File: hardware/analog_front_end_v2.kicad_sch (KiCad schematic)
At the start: 154 parts, among them J1 Conn_Coaxial, J3 Conn_01x01_Socket, J4 Conn_01x01_Socket, T1 WBC1-1TL 1:1, U1 ADL5531, U10 MAX6002, U11 LP2985-5.0, U12 ADF4531, U14 LP2985-5.0, U15 LP2985-5.0, U17 LP2985-3.3, U18 PAT1220-C-0DB, U19 PAT1220-C-0DB, U2 ADL5531, U20 PAT1220-C-0DB, U21 PAT1220-C-0DB, U22 MCP6286, U23 PMOD 2x6 2.54mm pitch, U24 LT5560, U25 LTC6362, U26 LTC6362, U3 ADL5531, U4 ADL5531, U5 LP2985-1.8, U6 MCP33131, U7 PAT1220-C-0DB, U9 PMOD 2x6 2.54mm pitch, Y1 12.8MHz TCXO

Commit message: Further schematic cleanups
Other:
- note removed: "TODO: Recheck if this gain amount is correct for the new downmixer and ADC"
- moved on the sheet: C10, C11, C12, C13, C14, C15, C16, C17, C18, C19, C2, C20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

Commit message: Further refinements/cleanup to Downmixer schematic section
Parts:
- removed C84: 10n, Capacitor_SMD:C_0402_1005Metric, symbol Device:C
- removed C85: 10u, Capacitor_SMD:C_0402_1005Metric, symbol Device:C
- removed C86: 100n, Capacitor_SMD:C_0402_1005Metric, symbol Device:C
- removed TP23: LOCK_DET, TestPoint:TestPoint_Pad_D1.0mm, symbol Connector:TestPoint
- added C22: 1u_16V, Capacitor_SMD:C_0603_1608Metric, symbol Device:C
- added C50: 10u_16V, Capacitor_SMD:C_0805_2012Metric, symbol Device:C
- added C51: 10n_25V, Capacitor_SMD:C_0402_1005Metric, symbol Device:C
- C87, C92, C93, C94: value 100n -> 100n_25V; MOC (none) -> GCM155R71E104KE02D; Size (none) -> 0402; Tolerance (none) -> 5%
- C88: value 1u -> 100n_25V; MOC (none) -> GCM155R71E104KE02D; Size (none) -> 0402; Tolerance (none) -> 5%
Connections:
- net 3V3: now also C22.1; no longer C88.1
- net ADC_SDO: no longer U23.7
- net GND: now also C22.2, C50.1, C51.1
- net PLL_TEMP: now also C93.1; no longer C94.1
- net PLL_VCOM: now also C92.1; no longer C93.1
- net PLL_VREF: now also C88.1; no longer C92.1
- net at FB1.1, U15.5 (VOUT): now also C94.1, C50.2
- net VCO_LD: now reaches U12.25 (LD)
- net VCO_LD: now also U23.7
- net at U15.4 (BP): now also C51.2
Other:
- note added: "Always on, don't care about power drain..."
- note added: "Goals: 1. Cover typical FM range 88 to 108MHz with 95 to 105 best covered 2. Support from -100dBm received signal 3. 50 ohm impedance 4. Minimize parasitics (inc trace resistance) as much as possible in layout 5. Short traces with minimal direction changes"
- note added: "TODO: Assign parts and tolerances!"
- note removed: "EN > 2V for ON"
- note removed: "Goals: 1. Support from -95dBm received signal 2. 50 ohm impedance 3. Minimize parasitics (inc trace resistance) as much as possible in layout 4. Short traces with minimal direction changes"
- note removed: "V_CM buffered by U22 (MCP6286)"
- moved on the sheet: C1, C10, C11, C12, C13, C14, C15, C16, C17, C18, C19, C2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

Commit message: Assign more values to downmixer and butterworth filters
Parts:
- removed C61, C62: 10n, Capacitor_SMD:C_0402_1005Metric, symbol Device:C
- removed C64, C67: 1n, Capacitor_SMD:C_0402_1005Metric, symbol Device:C
- removed C65, C66, C68, C80, C82: 100n, Capacitor_SMD:C_0402_1005Metric, symbol Device:C
- removed C69, C78, C79, C81, C83: 1u, Capacitor_SMD:C_0402_1005Metric, symbol Device:C
- added C23, C26, C29, C37, C39: 1u_16V, Capacitor_SMD:C_0603_1608Metric, symbol Device:C
- added C24, C25: 1n_50V, Capacitor_SMD:C_0402_1005Metric, symbol Device:C
- added C34, C35: 10n_25V, Capacitor_SMD:C_0402_1005Metric, symbol Device:C
- added C95, C96, C97, C98, C99: 100n_25V, Capacitor_SMD:C_0402_1005Metric, symbol Device:C
- C59: MOC (none) -> 0402N270FW201-T500; Size (none) -> 0402; Tolerance (none) -> 1%
- L13, L14: MOC (none) -> LQW15AN18NG8ZD; Tolerance (none) -> 2%
- R32: MOC (none) -> RC0402FR-13162RL; Size (none) -> 0402; Tolerance (none) -> 1%
- R33, R34: MOC (none) -> RC0402FR-07330RL; Size (none) -> 0402; Tolerance (none) -> 1%
- R35, R36, R37, R38, R41, R42, R43, R44: MOC (none) -> RT0402BRD071KL; Size (none) -> 0402; Tolerance (none) -> 1%
- T1: MOC (none) -> ADT1-1+
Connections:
- net 5V_MIX: now also C23.1, C24.1, C37.1, C39.1, C97.1, C98.1, C99.1
- net ADC_VCM: now also C29.1
- net GND: now also C23.2, C24.2, C26.2, C29.2, C35.1, C37.2, C39.2, C97.2, C98.2, C99.2
- net IF_N: now also C95.2
- net IF_P: now also C96.2
- net VCM_DIV: now also C26.1
- net at C63.2, R32.1: now also C34.2
- net at U24.1 (LO-): now also C34.1
- net at R33.2, U24.6 (OUT+): now also C25.1, C96.1
- net at R34.1, U24.5 (OUT-): now also C25.2, C95.1
- net at U24.8 (LO+): now also C35.2
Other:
- note added: "TODO: Assign Ferrite part!"
- note added: "TODO: Create footprint!"
- moved on the sheet: C1, C10, C11, C12, C13, C14, C15, C16, C17, C18, C19, C2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

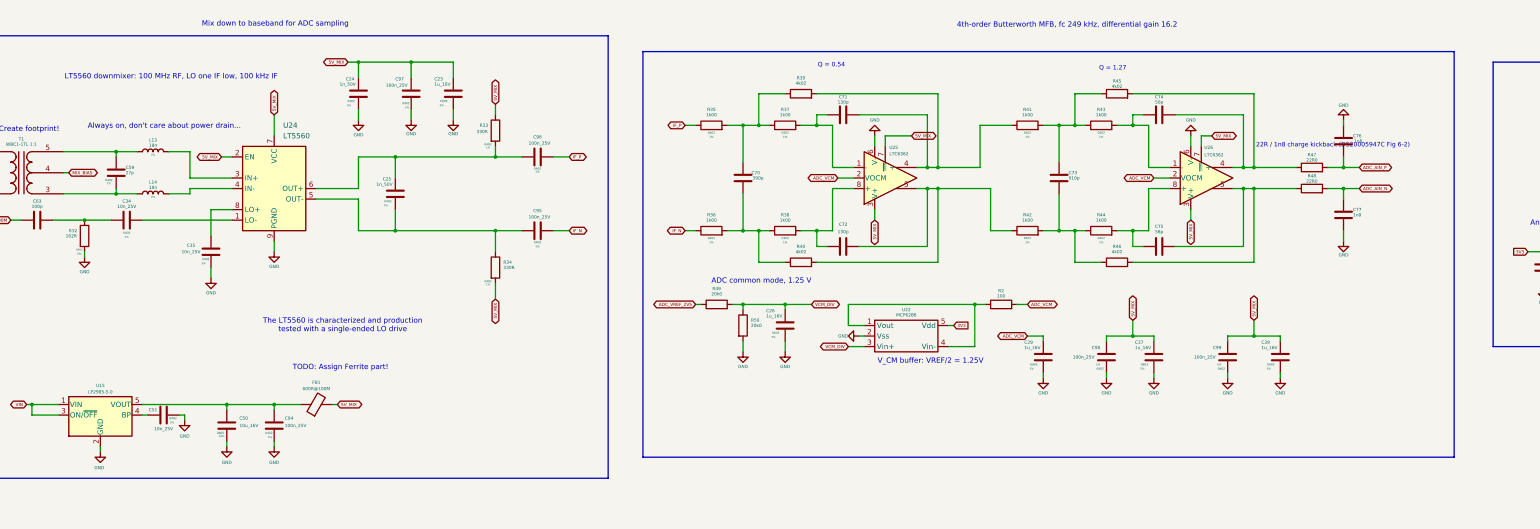
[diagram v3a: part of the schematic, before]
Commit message: Populate more components
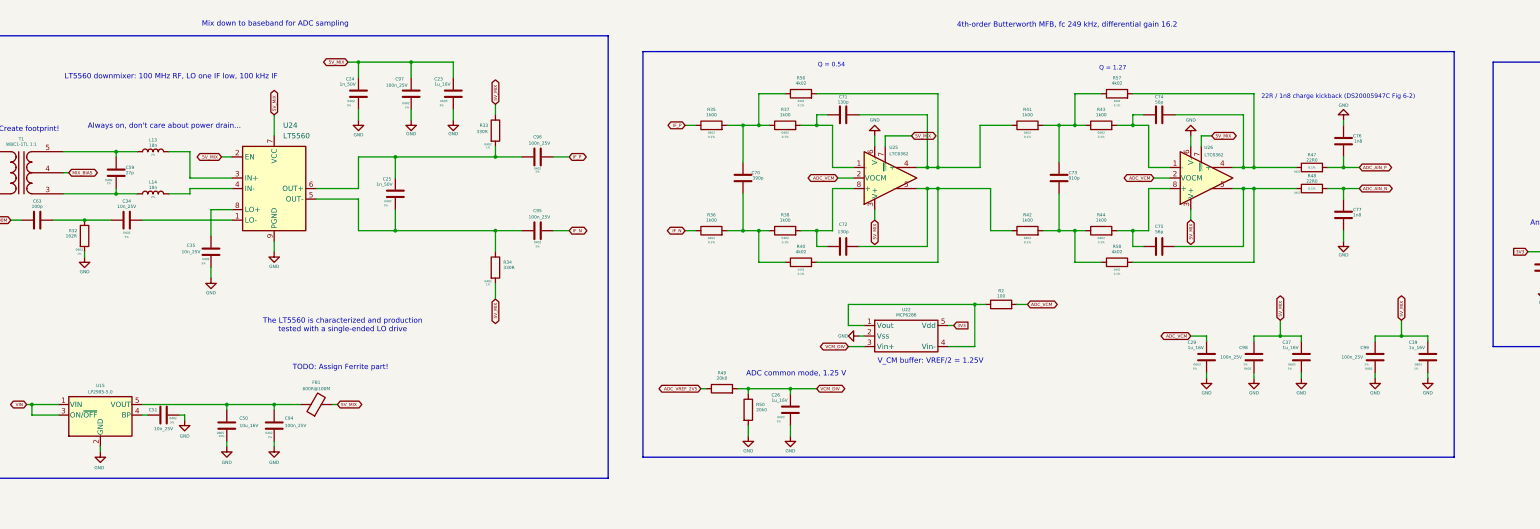
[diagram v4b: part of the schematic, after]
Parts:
- removed R39, R45, R46: 4k02, Resistor_SMD:R_0402_1005Metric, symbol Device:R
- added R56, R57, R58: 4k02, Resistor_SMD:R_0402_1005Metric, symbol Device:R
- R35, R36, R37, R38, R41, R42, R43, R44: Tolerance 1% -> 0.1%
- R40: MOC (none) -> RT0402BRD074K02L; Size (none) -> 0402; Tolerance (none) -> 0.1%
- R47, R48: MOC (none) -> RT0402BRD0722RL; Size (none) -> 0402; Tolerance (none) -> 0.1%
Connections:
- net at C73.2, R42.2, R44.1: now also R58.1
- net at C70.1, R35.2, R37.1: now also R56.1
- net at C71.2, R41.1, U25.4 (+): now also R56.2
- net at C73.1, R41.2, R43.1: now also R57.1
- net at C75.2, R48.1, U26.5 (-): now also R58.2
- net at C74.2, R47.1, U26.4 (+): now also R57.2
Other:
- moved on the sheet: C26, C29, C37, C39, C98, C99, R49, R50

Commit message: Populate more components
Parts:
- removed FB1: 600R@100M, Inductor_SMD:L_0402_1005Metric, symbol Device:FerriteBead
- removed R51: 50R, Resistor_SMD:R_0402_1005Metric, symbol Device:R
- added R59: 50R, Resistor_SMD:R_0402_1005Metric, symbol Device:R
- C70: MOC (none) -> GCM1555C1H391FA16D; Size (none) -> 0402; Tolerance (none) -> 1%
- C71, C72: MOC (none) -> GRT1555C1H131FA02D; Size (none) -> 0402; Tolerance (none) -> 1%
- C73: MOC (none) -> GCM1555C1H911FA16J; Size (none) -> 0402; Tolerance (none) -> 1%
- C74, C75: MOC (none) -> GCM1555C1H560FA16D; Size (none) -> 0402; Tolerance (none) -> 0.1%
- L13, L14: Size (none) -> 0402
- R52: MOC (none) -> RN73R1ETTP50R0F50; Size (none) -> 0402; Tolerance (none) -> 1%
- R53: MOC (none) -> RT0402BRD0733RL; Size (none) -> 0402; Tolerance (none) -> 0.1%
- R54: MOC (none) -> ERA-2AEB1371X; Size (none) -> 0402; Tolerance (none) -> 0.1%
- R55: MOC (none) -> RT0402BRD076K19L; Size (none) -> 0402; Tolerance (none) -> 0.1%
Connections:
- net 3V3: now also R59.1
- net 5V_MIX: now also C50.2, C94.1, U15.5 (VOUT)
- net LO_100M: now also R59.2
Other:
- note removed: "TODO: Assign Ferrite part!"
- moved on the sheet: C23, C24, C35, C95, C96, C97, R34

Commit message: Update more passive MOC/Size/tolerances across the schematic
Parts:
- C76, C77: MOC (none) -> GRM1885C1H182JA01D; Size (none) -> 0603; Tolerance (none) -> 5%
- R2: Size (none) -> 0402; Tolerance (none) -> 0.1%
- R49, R50: MOC (none) -> RC0402FR-0720KL; Size (none) -> 0402; Tolerance (none) -> 1%
- T1: footprint (none) -> fm-radio-footprint-lib:WBC1-1TLC; MOC ADT1-1+ -> WBC1-1TLC
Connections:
- net GND: now also R50.1; no longer R50.2
- net VCM_DIV: now also R50.2; no longer R50.1
- no-connect marks 29 -> 30
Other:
- moved on the sheet: C1, C2, C3, C4, C5, J1, L1, L2, L3, L4, L5, R32

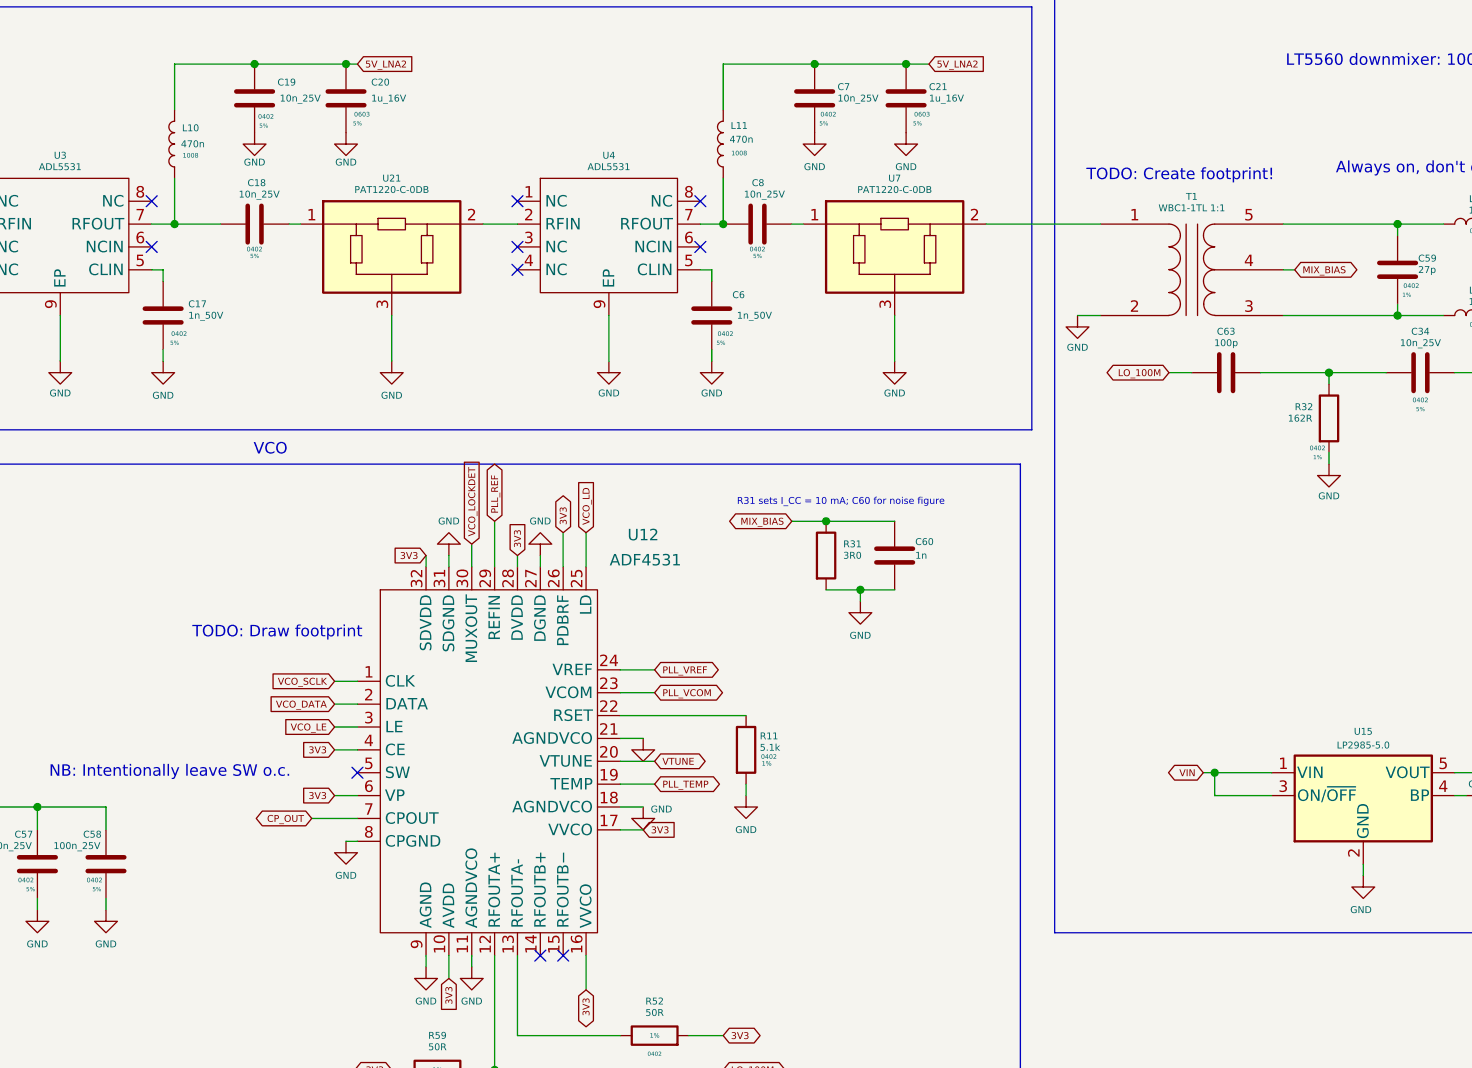
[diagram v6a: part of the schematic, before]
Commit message: More routing and move frontend inductor to be perpendicular
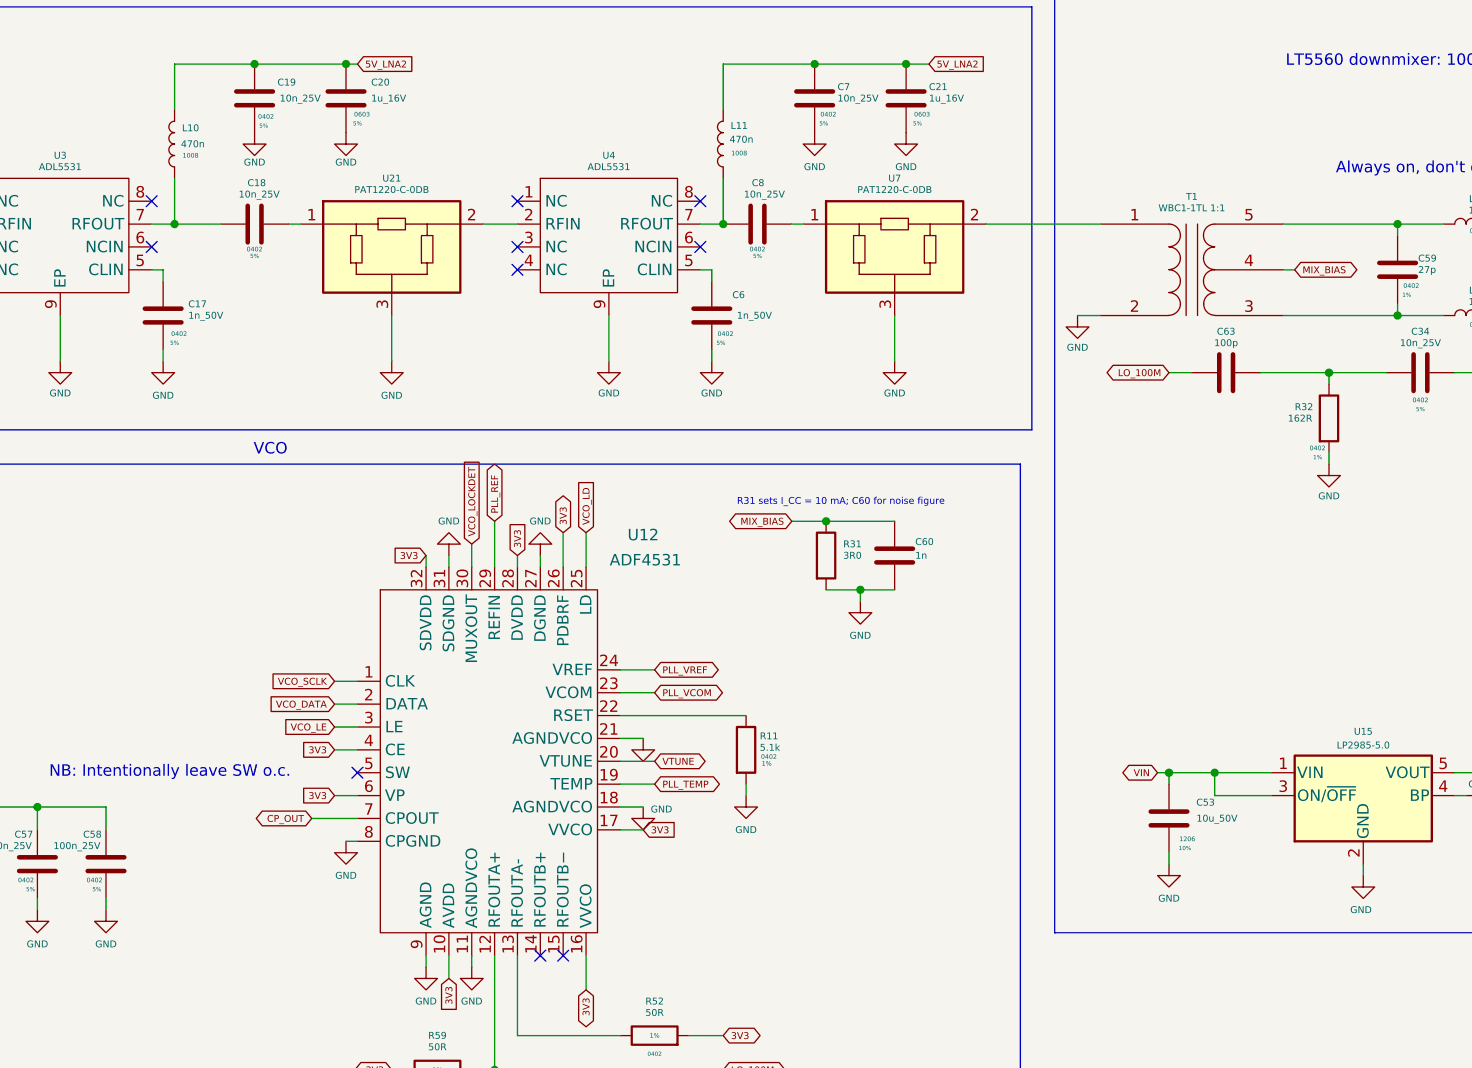
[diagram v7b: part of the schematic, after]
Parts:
- added C53: 10u_50V, Capacitor_SMD:C_1206_3216Metric, symbol Device:C
- U12: footprint (none) -> fm-radio-footprint-lib:ADF4351_LFCSP-32_5x5mm_P0.5mm_EP3.1x3.1mm
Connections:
- net GND: now also C53.1
- net VIN: now also C53.2
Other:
- note removed: "TODO: Create footprint!"
- note removed: "TODO: Draw footprint"

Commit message: Updated schematics/PCB files
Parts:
- removed C94: 100n_25V, Capacitor_SMD:C_0402_1005Metric, symbol Device:C
- added C61, C62, C64: 100n_25V, Capacitor_SMD:C_0402_1005Metric, symbol Device:C
- added C65: 47u_16V, Capacitor_Tantalum_SMD:CP_EIA-6032-15_Kemet-U, symbol Device:C_Polarized_US
- added R8: 0R, Resistor_SMD:R_0402_1005Metric, symbol Device:R
- C60: value 1n -> 1n_50V; MOC (none) -> GRM1555C1H102JA01D; Size (none) -> 0402; Tolerance (none) -> 5%
- C63: value 100p -> 100p_250V; MOC (none) -> 0603J2500101JHT; Size (none) -> 0603; Tolerance (none) -> 5%
- C89: MOC (none) -> C0402C152F5GECAUTO; Size (none) -> 0402; Tolerance (none) -> 1%
- C90: footprint Capacitor_SMD:C_0402_1005Metric -> Capacitor_SMD:C_0603_1608Metric; Size (none) -> 0603; Tolerance (none) -> 1%
- C91: Size (none) -> 0402; Tolerance (none) -> 1%
- R31: footprint Resistor_SMD:R_0402_1005Metric -> Resistor_SMD:R_0805_2012Metric; Size (none) -> 0805; Tolerance (none) -> 0.1%
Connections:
- net 3V3: now also C61.1, C62.1, C64.1
- net 5V_MIX: now also C65.1, R8.2; no longer C50.2, U15.5 (VOUT)
- net GND: now also C61.2, C62.2, C64.2, C65.2
- new net: C50.2, R8.1, U15.5 (VOUT)
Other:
- note removed: "TODO: Assign parts and tolerances!"
- moved on the sheet: C27, C28, C50, C51, C52, C54, C55, C56, C57, C58, C8, R31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
